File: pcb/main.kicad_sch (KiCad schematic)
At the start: 1 part

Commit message: moved stuff around
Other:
- sheet ADC ports: added +3V3, GND; removed none
- sheet Display ports: added +3V3, GND; removed none
- sheet Module Bay 0 ports: added +3V3, GND; removed none
- sheet Module Bay 1 ports: added +3V3, GND; removed none
- sheet RP2354B ports: added +3V3, GND; removed none
- sheet USB ports: added GND; removed none
- moved on the sheet: BT1

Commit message: did some layout
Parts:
- BT1: footprint Connector_JST:JST_PH_S2B-PH-SM4-TB_1x02-1MP_P2.00mm_Horizontal -> Connector_Molex:Molex_PicoBlade_53261-0271_1x02-1MP_P1.25mm_Horizontal
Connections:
- net GND: now also BT1.1 (-); no longer BT1.2 (-)
- net Power/+BATT: now also BT1.2 (+); no longer BT1.1 (+)
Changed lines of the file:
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@@
 			)
 		)
-		(property "Footprint" "Connector_JST:JST_PH_S2B-PH-SM4-TB_1x02-1MP_P2.00mm_Horizontal"
+		(property "Footprint" "Connector_Molex:Molex_PicoBlade_53261-0271_1x02-1MP_P1.25mm_Horizontal"
 			(at 107.315 121.666 90)
 			(hide yes)

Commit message: did more layout, added 3d models
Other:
- sheet Power ports: added GND; removed none
- moved on the sheet: BT1
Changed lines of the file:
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@@
 	(generator_version "10.0")
 	(paper "A4")
+	(junction
+		(at 102.87 127)
+		(diameter 0)
+		(color 0 0 0 0)
+	)
 	(wire
 		(pts
@@
 	(wire
 		(pts
-			(xy 107.315 116.84) (xy 111.125 116.84)
+			(xy 102.87 116.84) (xy 110.49 116.84)
 		)
 		(stroke
@@
 	(wire
 		(pts
+			(xy 110.49 120.65) (xy 107.95 120.65)
+		)
+		(stroke
+			(width 0)
+			(type default)
+		)
+	)
+	(wire
+		(pts
 			(xy 179.705 102.87) (xy 180.975 102.87)
 		)
@@
 	(wire
 		(pts
-			(xy 107.315 125.73) (xy 107.315 127)
+			(xy 102.87 125.73) (xy 102.87 127)
 		)
 		(stroke
@@
 	(wire
 		(pts
-			(xy 92.71 111.76) (xy 111.125 111.76)
-		)
-		(stroke
-			(width 0)
-			(type default)
-		)
-	)
-	(wire
-		(pts
-			(xy 107.315 116.84) (xy 107.315 118.11)
+			(xy 92.71 111.76) (xy 110.49 111.76)
+		)
+		(stroke
+			(width 0)
+			(type default)
+		)
+	)
+	(wire
+		(pts
+			(xy 102.87 116.84) (xy 102.87 118.11)
 		)
 		(stroke
@@
 	(wire
 		(pts
+			(xy 107.95 127) (xy 102.87 127)
+		)
+		(stroke
+			(width 0)
+			(type default)
+		)
+	)
+	(wire
+		(pts
 			(xy 146.05 59.69) (xy 181.61 59.69)
 		)
@@
 		(pts
 			(xy 146.05 87.63) (xy 180.975 87.63)
+		)
+		(stroke
+			(width 0)
+			(type default)
+		)
+	)
+	(wire
+		(pts
+			(xy 107.95 120.65) (xy 107.95 127)
 		)
 		(stroke
@@
 	(symbol
 		(lib_id "power:GND")
-		(at 107.315 127 0)
+		(at 102.87 127 0)
 		(unit 1)
 		(body_style 1)
@@
 		(dnp no)
 		(property "Reference" "#PWR050"
-			(at 107.315 133.35 0)
+			(at 102.87 133.35 0)
 			(hide yes)
 			(show_name no)
@@
 		)
 		(property "Value" "GND"
-			(at 107.315 131.572 0)
+			(at 102.87 131.572 0)
 			(show_name no)
 			(do_not_autoplace no)
@@
 		)
 		(property "Footprint" ""
-			(at 107.315 127 0)
+			(at 102.87 127 0)
 			(hide yes)
 			(show_name no)
@@
 		)
 		(property "Datasheet" ""
-			(at 107.315 127 0)
+			(at 102.87 127 0)
 			(hide yes)
 			(show_name no)
@@
 		)
 		(property "Description" "Power symbol creates a global label with name \"GND\" , ground"
-			(at 107.315 127 0)
+			(at 102.87 127 0)
 			(hide yes)
 			(show_name no)
@@
 	(symbol
 		(lib_id "Device:Battery_Cell")
-		(at 107.315 123.19 0)
+		(at 102.87 123.19 0)
 		(mirror y)
 		(unit 1)
@@
 		(dnp no)
 		(property "Reference" "BT1"
-			(at 103.505 120.0784 0)
+			(at 99.06 120.0784 0)
 			(show_name no)
 			(do_not_autoplace no)
@@
 		)
 		(property "Value" "Battery_Cell"
-			(at 103.505 122.6184 0)
+			(at 99.06 122.6184 0)
 			(show_name no)
 			(do_not_autoplace no)
@@
 		)
 		(property "Footprint" "Connector_Molex:Molex_PicoBlade_53261-0271_1x02-1MP_P1.25mm_Horizontal"
-			(at 107.315 121.666 90)
+			(at 102.87 121.666 90)
 			(hide yes)
 			(show_name no)
@@
 		)
 		(property "Datasheet" ""
-			(at 107.315 121.666 90)
+			(at 102.87 121.666 90)
 			(hide yes)
 			(show_name no)
@@
 		)
 		(property "Description" "Single-cell battery"
-			(at 107.315 123.19 0)
+			(at 102.87 123.19 0)
 			(hide yes)
 			(show_name no)
@@
 		)
 		(property "Sim.Device" "V"
-			(at 107.315 123.19 0)
+			(at 102.87 123.19 0)
 			(hide yes)
 			(show_name no)
@@
 		)
 		(property "Sim.Type" "DC"
-			(at 107.315 123.19 0)
+			(at 102.87 123.19 0)
 			(hide yes)
 			(show_name no)
@@
 		)
 		(property "Sim.Pins" "1=+ 2=-"
-			(at 107.315 123.19 0)
+			(at 102.87 123.19 0)
 			(hide yes)
 			(show_name no)
@@
 		)
 		(property "LCSC" "C295747"
-			(at 107.315 123.19 0)
+			(at 102.87 123.19 0)
 			(hide yes)
 			(show_name no)
@@
 	)
 	(sheet
-		(at 111.125 109.855)
-		(size 12.7 8.255)
+		(at 110.49 109.855)
+		(size 13.335 12.065)
 		(exclude_from_sim no)
 		(in_bom yes)
@@
 		)
 		(property "Sheetname" "Power"
-			(at 111.125 109.1434 0)
+			(at 110.49 109.1434 0)
 			(show_name no)
 			(do_not_autoplace no)
@@
 		)
 		(property "Sheetfile" "pwr.kicad_sch"
-			(at 111.125 118.6946 0)
+			(at 110.49 122.5046 0)
 			(show_name no)
 			(do_not_autoplace no)
@@
 		)
 		(pin "+BATT" input
-			(at 111.125 116.84 180)
+			(at 110.49 116.84 180)
 			(effects
 				(font
@@
 		)
 		(pin "VBUS" input
-			(at 111.125 111.76 180)
+			(at 110.49 111.76 180)
 			(effects
 				(font
@@
 			)
 		)
+		(pin "GND" input
+			(at 110.49 120.65 180)
+			(effects
+				(font
+					(size 1.27 1.27)
+				)
+				(justify left)
+			)
+		)

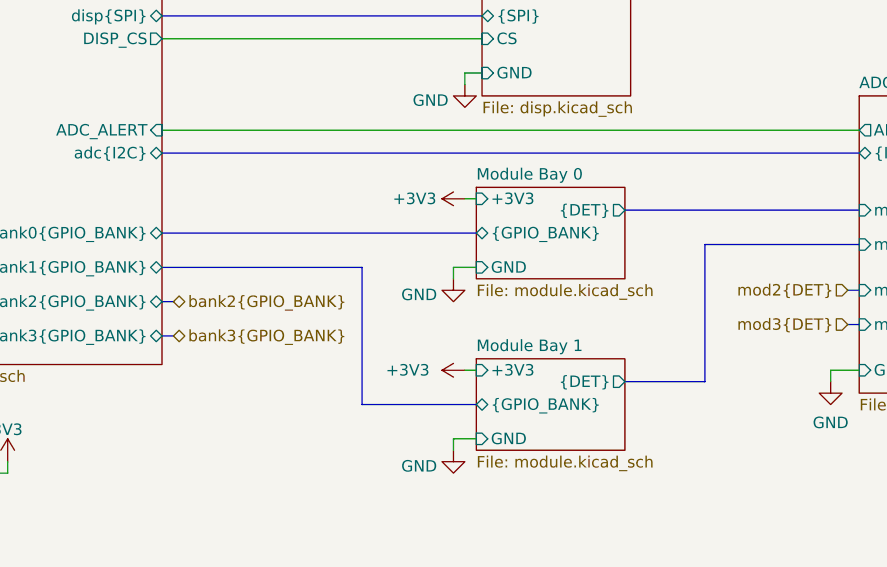
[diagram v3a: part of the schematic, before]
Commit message: swapped the module pins around
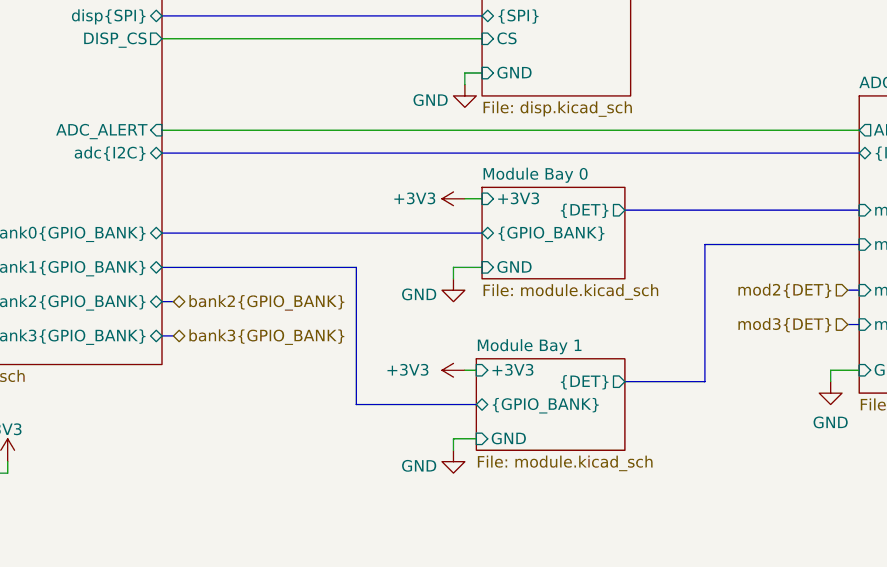
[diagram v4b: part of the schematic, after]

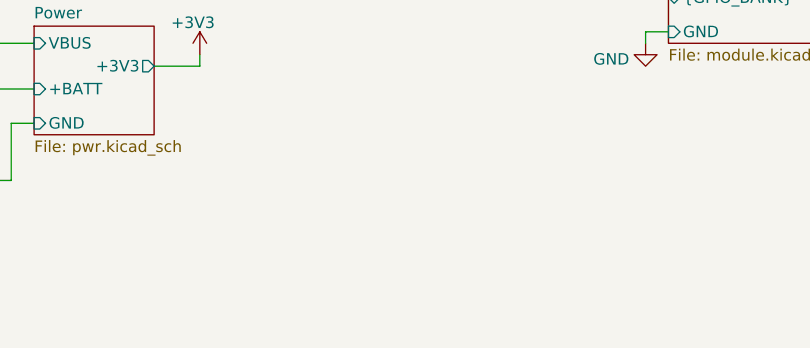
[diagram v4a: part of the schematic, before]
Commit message: added mounting holes
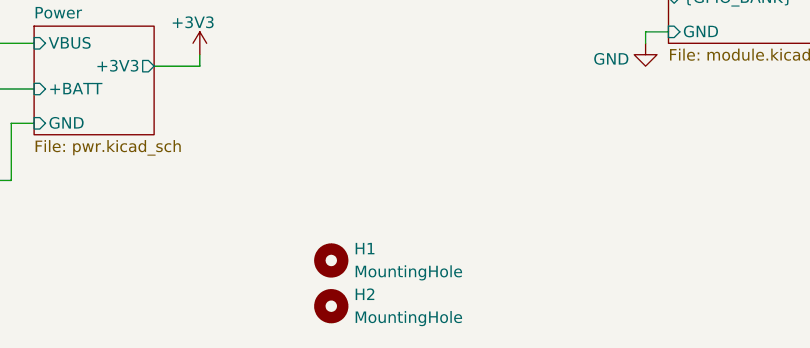
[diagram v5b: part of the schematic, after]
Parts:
- added H1, H2: MountingHole, MountingHole:MountingHole_2.2mm_M2, symbol Mechanical:MountingHole
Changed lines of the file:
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@@
+	)
+	(symbol
+		(lib_id "Mechanical:MountingHole")
+		(at 143.51 135.89 0)
+		(unit 1)
+		(body_style 1)
+		(exclude_from_sim no)
+		(in_bom no)
+		(on_board yes)
+		(in_pos_files yes)
+		(dnp no)
+		(fields_autoplaced yes)
+		(property "Reference" "H1"
+			(at 146.05 134.6199 0)
+			(show_name no)
+			(do_not_autoplace no)
+			(effects
+				(font
+					(size 1.27 1.27)
+				)
+				(justify left)
+			)
+		)
+		(property "Value" "MountingHole"
+			(at 146.05 137.1599 0)
+			(show_name no)
+			(do_not_autoplace no)
+			(effects
+				(font
+					(size 1.27 1.27)
+				)
+				(justify left)
+			)
+		)
+		(property "Footprint" "MountingHole:MountingHole_2.2mm_M2"
+			(at 143.51 135.89 0)
+			(hide yes)
+			(show_name no)
+			(do_not_autoplace no)
+			(effects
+				(font
+					(size 1.27 1.27)
+				)
+			)
+		)
+		(property "Datasheet" ""
+			(at 143.51 135.89 0)
+			(hide yes)
+			(show_name no)
+			(do_not_autoplace no)
+			(effects
+				(font
+					(size 1.27 1.27)
+				)
+			)
+		)
+		(property "Description" "Mounting Hole without connection"
+			(at 143.51 135.89 0)
+			(hide yes)
+			(show_name no)
+			(do_not_autoplace no)
+			(effects
+				(font
+					(size 1.27 1.27)
+				)
+			)
+		)
+		(instances
+			(project "hackxpansion"
+				(path "/aaf5804d-3f78-442b-969e-39faa388db94/61af021d-ad04-487f-9d02-e2b100ecd1ae"
+					(reference "H1")
+					(unit 1)
+				)
+			)
+		)
 	)
 	(symbol
@@
 					(unit 1)
 				)
+			)
+		)
+	)
+	(symbol
+		(lib_id "Mechanical:MountingHole")
+		(at 143.51 140.97 0)
+		(unit 1)
+		(body_style 1)
+		(exclude_from_sim no)
+		(in_bom no)
+		(on_board yes)
+		(in_pos_files yes)
+		(dnp no)
+		(fields_autoplaced yes)
+		(property "Reference" "H2"
+			(at 146.05 139.6999 0)
+			(show_name no)
+			(do_not_autoplace no)
+			(effects
+				(font
+					(size 1.27 1.27)
+				)
+				(justify left)
+			)
+		)
+		(property "Value" "MountingHole"
+			(at 146.05 142.2399 0)
+			(show_name no)
+			(do_not_autoplace no)
+			(effects
+				(font
+					(size 1.27 1.27)
+				)
+				(justify left)
+			)
+		)
+		(property "Footprint" "MountingHole:MountingHole_2.2mm_M2"
+			(at 143.51 140.97 0)
+			(hide yes)
+			(show_name no)
+			(do_not_autoplace no)
+			(effects
+				(font
+					(size 1.27 1.27)
+				)
+			)
+		)
+		(property "Datasheet" ""
+			(at 143.51 140.97 0)
+			(hide yes)
+			(show_name no)
+			(do_not_autoplace no)
+			(effects
+				(font
+					(size 1.27 1.27)
+				)
+			)
+		)
+		(property "Description" "Mounting Hole without connection"
+			(at 143.51 140.97 0)
+			(hide yes)
+			(show_name no)
+			(do_not_autoplace no)
+			(effects
+				(font
+					(size 1.27 1.27)
+				)
+			)
+		)
+		(instances
+			(project "hackxpansion"
+				(path "/aaf5804d-3f78-442b-969e-39faa388db94/61af021d-ad04-487f-9d02-e2b100ecd1ae"
+					(reference "H2")
+					(unit 1)
+				)

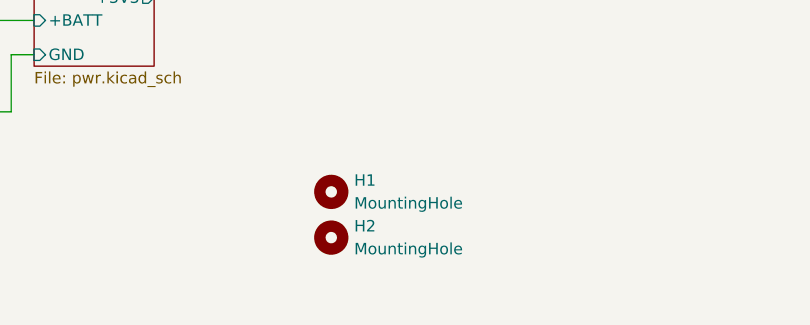
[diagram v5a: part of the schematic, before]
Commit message: finished daughter board, added stuff to main board
added esd and extra mounting hole to mainboard, finished daughter board
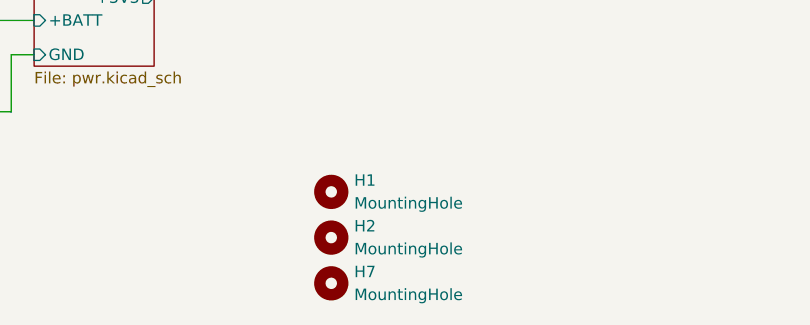
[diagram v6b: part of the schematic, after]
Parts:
- added H7: MountingHole, MountingHole:MountingHole_2.2mm_M2, symbol Mechanical:MountingHole
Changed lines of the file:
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@@
+	)
+	(symbol
+		(lib_id "Mechanical:MountingHole")
+		(at 143.51 146.05 0)
+		(unit 1)
+		(body_style 1)
+		(exclude_from_sim no)
+		(in_bom no)
+		(on_board yes)
+		(in_pos_files yes)
+		(dnp no)
+		(fields_autoplaced yes)
+		(property "Reference" "H7"
+			(at 146.05 144.7799 0)
+			(show_name no)
+			(do_not_autoplace no)
+			(effects
+				(font
+					(size 1.27 1.27)
+				)
+				(justify left)
+			)
+		)
+		(property "Value" "MountingHole"
+			(at 146.05 147.3199 0)
+			(show_name no)
+			(do_not_autoplace no)
+			(effects
+				(font
+					(size 1.27 1.27)
+				)
+				(justify left)
+			)
+		)
+		(property "Footprint" "MountingHole:MountingHole_2.2mm_M2"
+			(at 143.51 146.05 0)
+			(hide yes)
+			(show_name no)
+			(do_not_autoplace no)
+			(effects
+				(font
+					(size 1.27 1.27)
+				)
+			)
+		)
+		(property "Datasheet" ""
+			(at 143.51 146.05 0)
+			(hide yes)
+			(show_name no)
+			(do_not_autoplace no)
+			(effects
+				(font
+					(size 1.27 1.27)
+				)
+			)
+		)
+		(property "Description" "Mounting Hole without connection"
+			(at 143.51 146.05 0)
+			(hide yes)
+			(show_name no)
+			(do_not_autoplace no)
+			(effects
+				(font
+					(size 1.27 1.27)
+				)
+			)
+		)
+		(instances
+			(project "hackxpansion"
+				(path "/aaf5804d-3f78-442b-969e-39faa388db94/61af021d-ad04-487f-9d02-e2b100ecd1ae"
+					(reference "H7")
+					(unit 1)
+				)
+			)
+		)
 	)
 	(symbol
